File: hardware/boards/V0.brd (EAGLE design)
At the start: 45 x 104 mm, 142 parts, among them IC2 TPS6300, J12 3.5mm TRRS Jack, J2 HIROSE_DM3BT-DSF-PEJSHIROSE_D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, J3 MOLEX_105450-0101MOLEX_105450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, Q2 ON_SEMI_MMBT5551LT1GON_SEMI_M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, U1 VS1053-L, U2 MICROCHIP_MCP73831T-2ATI-OTMI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, X3 FH12-45S-0.5SH

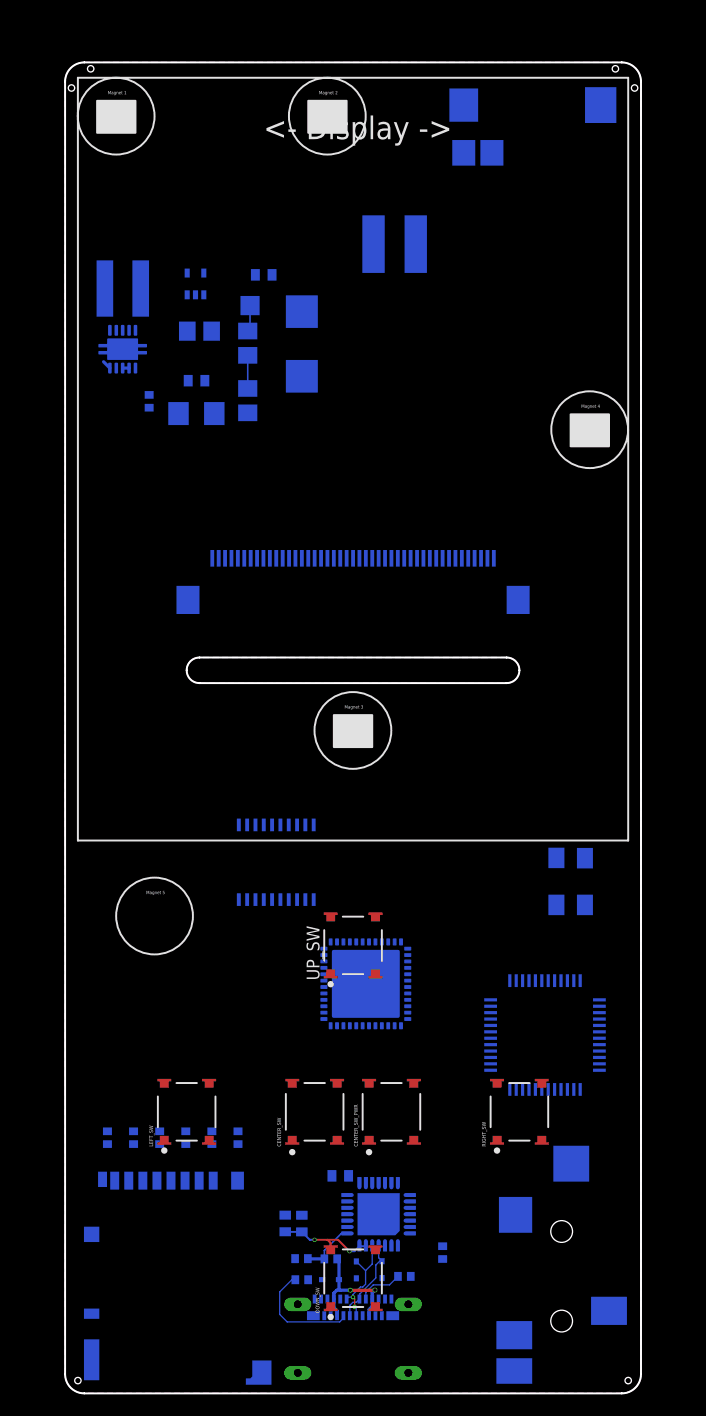
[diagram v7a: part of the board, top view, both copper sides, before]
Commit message: fix magnets (3mm _diameter_ - I hope)
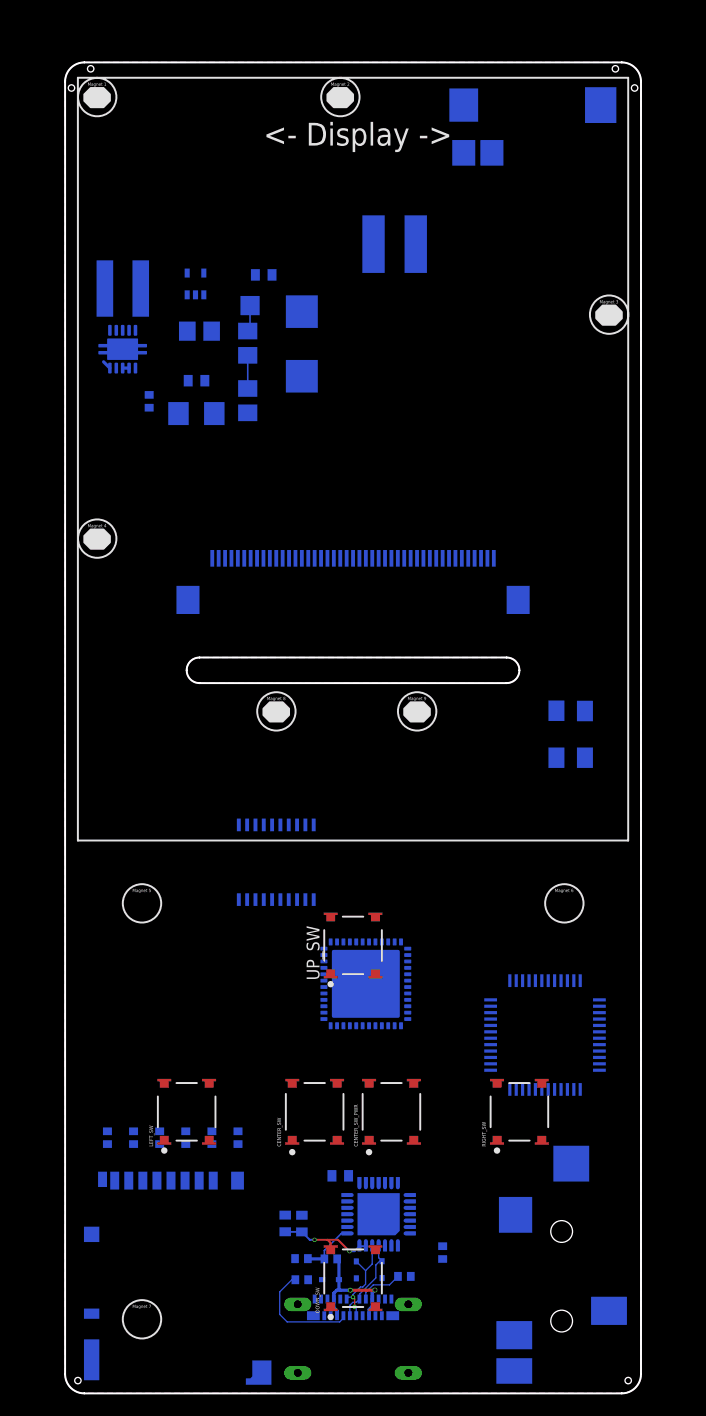
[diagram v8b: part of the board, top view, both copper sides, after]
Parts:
- moved U$4 11.5 mm to (17.0, -21.5)
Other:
- board text added: "Magnet 6"
- board text added: "Magnet 7"
- board text added: "Magnet 8"
- board text added: "Magnet 9"
